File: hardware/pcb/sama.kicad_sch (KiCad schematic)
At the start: 19 parts, among them J4 Conn_ARM_JTAG_SWD_10, U1 SAMA7D65-4HB, Y1 32kHz768, Y2 24MHz

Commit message: bunch of small changes
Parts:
- added JP3: JTAGSEL, symbol Jumper:SolderJumper_3_Bridged12
- R10: value 4k02 ± 1% -> 4k02
- R2: value 240R 1% -> 240R
- R9: value 5k62 ± 1% -> 5k62
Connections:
- net +1V8_BATT_CPU: now also JP3.1 (A); no longer U1.E8 (VBAT)
- net +3V3: now also JP3.3 (B)
- net BOOT.DAT1: now reaches U1.A13 (PB25)
- net BOOT.DAT2: now reaches U1.A15 (PB26)
- net BOOT.DAT0: now reaches U1.B15 (PB24)
- net BOOT.DAT3: now reaches U1.C11 (PB27)
- net BOOT.CMD: now reaches U1.C14 (PB22)
- net BOOT.CK: now reaches U1.D14 (PB23)
- net BOOT.CD: now reaches U1.G4 (PB29)
- net EXT.DAT1: now reaches U1.P16 (PA4)
- net EXT.DAT3: now reaches U1.R12 (PA10)
- net EXT.DAT0: now reaches U1.T18 (PA3)
- net EXT.DAT2: now reaches U1.U14 (PA9)
- net EXT.CK: now reaches U1.U18 (PA0)
- net EXT.CD: now reaches U1.V15 (PA16)
- net EXT.CMD: now reaches U1.V17 (PA1)
- net UART_SAMBA_RX: now reaches U1.F18 (PD19)
- net UART_SAMBA_TX: now reaches U1.H16 (PD18)
- new net: JP3.2 (C), U1.E8 (VBAT)
- no-connect marks 27 -> 38
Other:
- moved on the sheet: U1D

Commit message: bunch of small audio and rf changes
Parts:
- added J8: Conn_01x02_Pin, symbol Connector:Conn_01x02_Pin
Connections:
- net UART_SAMBA_RX: now also J8.2 (Pin_2)
- net UART_SAMBA_TX: now also J8.1 (Pin_1)
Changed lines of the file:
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@@
+	)
+	(symbol
+		(lib_id "Connector:Conn_01x02_Pin")
+		(at 99.06 139.7 0)
+		(mirror y)
+		(unit 1)
+		(body_style 1)
+		(exclude_from_sim no)
+		(in_bom yes)
+		(on_board yes)
+		(in_pos_files yes)
+		(dnp no)
+		(property "Reference" "J8"
+			(at 96.266 136.398 0)
+			(show_name no)
+			(do_not_autoplace no)
+			(effects
+				(font
+					(size 1.27 1.27)
+				)
+			)
+		)
+		(property "Value" "Conn_01x02_Pin"
+			(at 100.33 142.2399 0)
+			(hide yes)
+			(show_name no)
+			(do_not_autoplace no)
+			(effects
+				(font
+					(size 1.27 1.27)
+				)
+				(justify right)
+			)
+		)
+		(property "Footprint" ""
+			(at 99.06 139.7 0)
+			(hide yes)
+			(show_name no)
+			(do_not_autoplace no)
+			(effects
+				(font
+					(size 1.27 1.27)
+				)
+			)
+		)
+		(property "Datasheet" ""
+			(at 99.06 139.7 0)
+			(hide yes)
+			(show_name no)
+			(do_not_autoplace no)
+			(effects
+				(font
+					(size 1.27 1.27)
+				)
+			)
+		)
+		(property "Description" "Generic connector, single row, 01x02, script generated"
+			(at 99.06 139.7 0)
+			(hide yes)
+			(show_name no)
+			(do_not_autoplace no)
+			(effects
+				(font
+					(size 1.27 1.27)
+				)
+			)
+		)
+		(pin "1"
+		)
+		(pin "2"
+		)
+		(instances
+			(project "meko"
+				(path "/da54f10a-146b-4941-a9c7-55c7173bb101/11193406-550a-48b1-a654-5418a2035a4e"
+					(reference "J8")
+					(unit 1)
+				)
+			)
+		)
 	)
 	(symbol

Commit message: replaced lpddr3 with ddr3l
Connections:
- net DDR_A14: now reaches U1.L9 (DDR_A14)
- net DDR_A11: now reaches U1.M9 (DDR_A11)
- net ~{WE}: now reaches U1.N10 (DDR_WEN)
- net BA1: now reaches U1.P4 (DDR_BA1)
- net DDR_A12: now reaches U1.P5 (DDR_A12)
- net BA2: now reaches U1.R8 (DDR_BA2)
- net DDR_A10: now reaches U1.T3 (DDR_A10)
- net ~{CAS}: now reaches U1.T8 (DDR_CASN)
- net ~{RAS}: now reaches U1.U8 (DDR_RASN)
- net ~{RESET}: now reaches U1.V1 (DDR_RESETN)
- net DDR_A13: now reaches U1.V2 (DDR_A13)
- net BA0: now reaches U1.V8 (DDR_BA0)
- net +1V2_DDR renamed +1V35_DDR
- no-connect marks 38 -> 26

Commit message: assigning pins
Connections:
- net +1V8: now also U1.F13 (VDDSDMMC2), U1.P19 (VDDQSPI0)
- net +3V3: now also U1.F9 (VDDSDMMC1), U1.W17 (VDDSDMMC0)
- net BT.HOST_WAKE: now reaches U1.L14 (PB19)
- net BT.DEV_WAKE: now reaches U1.M12 (PB20)
- net BT.DIN: now reaches U1.M14 (PB17)
- net BT.FSYNC: now reaches U1.M15 (PB15)
- net WL.EN: now reaches U1.N14 (PB13)
- net BT.BCLK: now reaches U1.N15 (PB14)
- net BT.DOUT: now reaches U1.N20 (PB16)
- net BT.MCLK: now reaches U1.N21 (PB18)
- net BT.CTSN: now reaches U1.P17 (PB10)
- net BT.RTSN: now reaches U1.P18 (PB12)
- net BT.RX: now reaches U1.R18 (PB9)
- net BT.EN: now reaches U1.R19 (PB11)
- net BT.TX: now reaches U1.T19 (PB8)
- net WIFI.DAT2: now reaches U1.A16 (PC31)
- net WIFI.DAT0: now reaches U1.B16 (PC29)
- net WIFI.CMD: now reaches U1.C15 (PC27)
- net WIFI.DAT3: now reaches U1.C16 (PD0)
- net WIFI.CK: now reaches U1.D16 (PC28)
- net WIFI.DAT1: now reaches U1.D17 (PC30)
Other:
- note added: "CTS"
- note added: "RTS"
- note added: "RX"
- note added: "TX"
- moved on the sheet: C27, J8, R10, R9, TP2, TP3, TP4, TP5, TP6, U1E, U1F

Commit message: connect everything up (Almost)
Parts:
- added R25, R36, R37, R40: 10k, symbol Device:R_Small
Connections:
- net +1V8: now also U1.C17 (VDDIOP1)
- net +3V3: now also U1.H19 (VDDGMAC1), U1.L19 (VDDGMAC0), U1.T13 (VDDIOP0), U1.W11 (VDDLVDS), R25.2, R36.2, R37.2, R40.2
- net CHG_~{INT}: now also U1.B19 (PD30)
- net CODEC.BCLK: now also U1.H4 (PC16)
- net CODEC.DIN: now also U1.D4 (PC17)
- net CODEC.DOUT: now also U1.J7 (PC14)
- net CODEC.FSYNC: now also U1.F3 (PC15)
- net DISP: now also U1.B21 (PA25)
- net FUEL_~{INT}: now also U1.F20 (PD31)
- net GPI1: now also U1.K9 (PD25)
- net GPIO1: now also U1.F19 (PD22)
- net GPIO2: now also U1.G18 (PD23)
- net GPO1: now also U1.G19 (PD24)
- net HAPT_EN: now also U1.Y19 (PE11)
- net HAPT_~{INT}: now also U1.AA19 (PE10)
- net HPM: now also U1.C1 (PC11)
- net SCL: now also U1.H6 (PC6), R37.1
- net SCLK: now also U1.P10 (PA22)
- net SCS: now also U1.AA20 (PA23)
- net SDA: now also U1.B1 (PC7), R40.1
- net SI: now also U1.P9 (PA24)
- net TOUCH.SCL: now also U1.K12 (PE2), R36.1
- net TOUCH.SDA: now also U1.D20 (PE3), R25.1
- net TOUCH_~{INT}: now also U1.Y15 (PE7)
- net TOUCH_~{RST}: now also U1.AA16 (PE8)
- net UART_SAMBA_RX: now also J8.1 (Pin_1), U1.H16 (PD18); no longer J8.2 (Pin_2), U1.F18 (PD19)
- net UART_SAMBA_TX: now also J8.2 (Pin_2), U1.F18 (PD19); no longer J8.1 (Pin_1), U1.H16 (PD18)
- net WL.DEV_WAKE: now also U1.G13 (PD2)
- net WL.HOST_WAKE: now also U1.A18 (PD1)
- net ~{DET}_2.5mm: now also U1.C2 (PC4)
- net ~{DET}_3.5mm: now also U1.G8 (PC3)
- net ~{INT}: now also U1.H5 (PC12)
- no-connect marks 26 -> 19
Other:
- note added: "DDR"
- note added: "GPIO"
- note added: "PERIs"
- note added: "PWR"
- note added: "SYS"
- moved on the sheet: C22, C23, C24, C25, C27, J4, J8, JP2, JP3, R10, R2, R9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

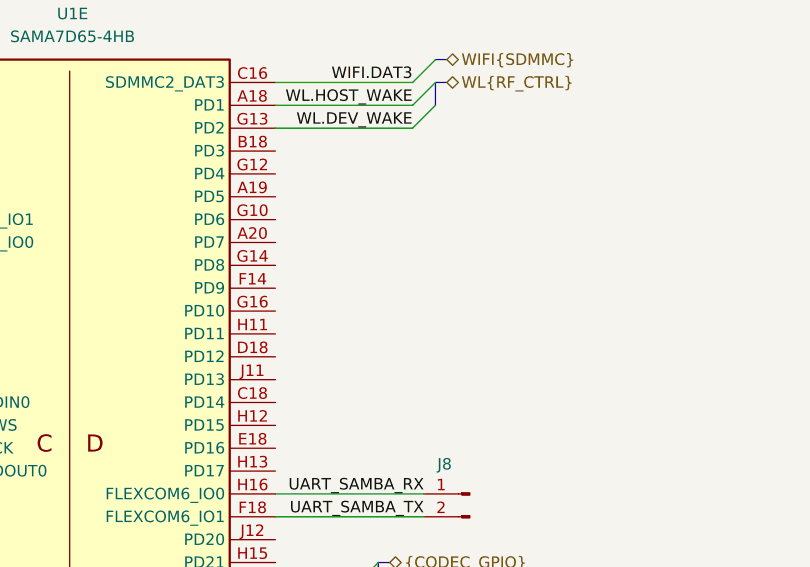
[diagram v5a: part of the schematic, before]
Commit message: added buttons
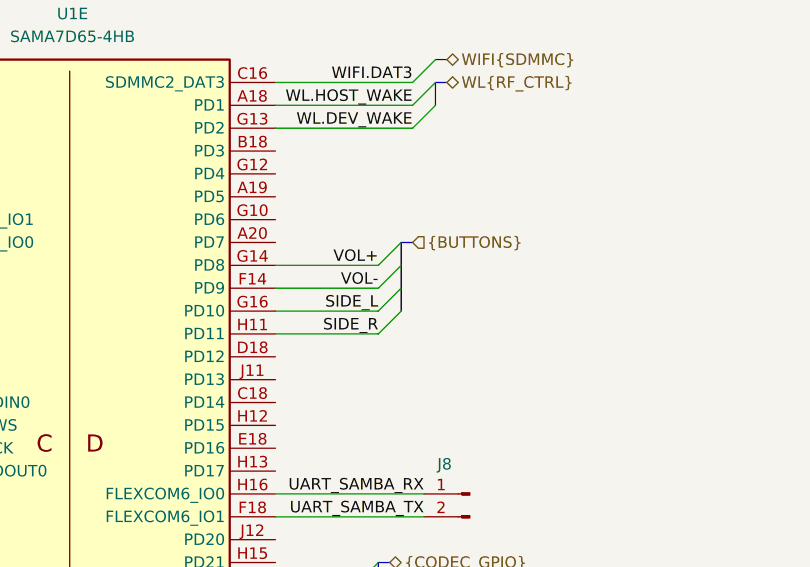
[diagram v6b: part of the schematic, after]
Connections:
- net VOL-: now reaches U1.F14 (PD9)
- net VOL+: now reaches U1.G14 (PD8)
- net SIDE_L: now reaches U1.G16 (PD10)
- net SIDE_R: now reaches U1.H11 (PD11)
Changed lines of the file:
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@@
 	)
 	(bus_entry
+		(at 130.81 73.66)
+		(size -2.54 2.54)
+		(stroke
+			(width 0)
+			(type default)
+		)
+	)
+	(bus_entry
 		(at 281.94 102.87)
 		(size -2.54 2.54)
@@
 	)
 	(bus_entry
+		(at 130.81 71.12)
+		(size -2.54 2.54)
+		(stroke
+			(width 0)
+			(type default)
+		)
+	)
+	(bus_entry
 		(at 463.55 107.95)
 		(size -2.54 2.54)
@@
 	)
 	(bus_entry
+		(at 130.81 68.58)
+		(size -2.54 2.54)
+		(stroke
+			(width 0)
+			(type default)
+		)
+	)
+	(bus_entry
 		(at 463.55 81.28)
 		(size -2.54 2.54)
@@
 	)
 	(bus_entry
+		(at 130.81 66.04)
+		(size -2.54 2.54)
+		(stroke
+			(width 0)
+			(type default)
+		)
+	)
+	(bus_entry
 		(at 463.55 68.58)
 		(size -2.54 2.54)
@@
 		)
 	)
+	(bus
+		(pts
+			(xy 130.81 66.04) (xy 130.81 73.66)
+		)
+		(stroke
+			(width 0)
+			(type default)
+		)
+	)
 	(wire
 		(pts
@@
 	(wire
 		(pts
+			(xy 116.84 73.66) (xy 128.27 73.66)
+		)
+		(stroke
+			(width 0)
+			(type default)
+		)
+	)
+	(wire
+		(pts
 			(xy 199.39 82.55) (xy 209.55 82.55)
 		)
@@
 	(bus
 		(pts
+			(xy 132.08 66.04) (xy 130.81 66.04)
+		)
+		(stroke
+			(width 0)
+			(type default)
+		)
+	)
+	(bus
+		(pts
 			(xy 283.21 74.93) (xy 281.94 74.93)
 		)
@@
 	(wire
 		(pts
+			(xy 116.84 71.12) (xy 128.27 71.12)
+		)
+		(stroke
+			(width 0)
+			(type default)
+		)
+	)
+	(wire
+		(pts
 			(xy 331.47 226.06) (xy 334.01 226.06)
 		)
@@
 	(wire
 		(pts
+			(xy 116.84 68.58) (xy 128.27 68.58)
+		)
+		(stroke
+			(width 0)
+			(type default)
+		)
+	)
+	(wire
+		(pts
 			(xy 151.13 227.33) (xy 165.1 227.33)
 		)
@@
 	(wire
 		(pts
+			(xy 116.84 76.2) (xy 128.27 76.2)
+		)
+		(stroke
+			(width 0)
+			(type default)
+		)
+	)
+	(wire
+		(pts
 			(xy 450.85 290.83) (xy 450.85 293.37)
 		)
@@
 		)
 	)
+	(label "SIDE_L"
+		(at 128.27 73.66 180)
+		(effects
+			(font
+				(size 1.27 1.27)
+			)
+			(justify right bottom)
+		)
+	)
 	(label "DQ5"
 		(at 461.01 68.58 180)
@@
 		)
 	)
+	(label "VOL-"
+		(at 128.27 71.12 180)
+		(effects
+			(font
+				(size 1.27 1.27)
+			)
+			(justify right bottom)
+		)
+	)
 	(label "DDR_A9"
 		(at 393.7 78.74 0)
@@
 		)
 	)
+	(label "VOL+"
+		(at 128.27 68.58 180)
+		(effects
+			(font
+				(size 1.27 1.27)
+			)
+			(justify right bottom)
+		)
+	)
 	(label "TDI"
 		(at 66.04 111.76 0)
@@
 		)
 	)
+	(label "SIDE_R"
+		(at 128.27 76.2 180)
+		(effects
+			(font
+				(size 1.27 1.27)
+			)
+			(justify right bottom)
+		)
+	)
 	(label "TDO"
 		(at 167.64 275.59 0)
@@
 		(effects
 			(font
+				(size 1.27 1.27)
+			)
+			(justify left)
+		)
+	)
+	(hierarchical_label "{BUTTONS}"
+		(shape input)
+		(at 132.08 66.04 0)
+		(effects
+			(font

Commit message: looking over stuff, added caps
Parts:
- added C100, C115, C119, C68, C83, C89, C90: 4u7, Capacitor_SMD:C_0402_1005Metric, symbol Device:C_Small
- added C101, C102, C103, C104, C105, C106, C107, C108, C109, C110, C111, C112, C113, C114, C116, C117, C118, C120, C121, C122, C123, C124, C125, C69, C70, C71, C72, C73, C74, C75, C76, C77, C78, C79, C80, C81, C82, C84, C85, C86, C87, C88, C91, C92, C93, C94, C95, C96, C97, C98, C99: 100n, Capacitor_SMD:C_0402_1005Metric, symbol Device:C_Small
- added R45, R46, R47, R48: 16k9, Resistor_SMD:R_0402_1005Metric, symbol Device:R_Small
- added TP7: ~{TRST}, symbol Connector:TestPoint
- C22, C23, C24, C25, C27: footprint (none) -> Capacitor_SMD:C_0402_1005Metric
- R10, R2, R25, R36, R37, R40, R9: footprint (none) -> Resistor_SMD:R_0402_1005Metric
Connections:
- net +1V15_CORE: now also C68.1, C69.1, C70.1, C71.1, C72.1, C73.1, C74.1, C75.1, C76.1, C77.1, C78.1, C79.1, C80.1, C81.1, C82.1
- net +1V15_CPU: now also C83.1, C84.1, C85.1, C86.1, C87.1, C88.1
- net +1V35_DDR: now also C100.1, C101.1, C102.1, C103.1, C104.1, C105.1, C106.1, C107.1, C108.1, C109.1, C110.1, C111.1, C112.1, C113.1, C114.1
- net +1V8: now also C115.1, C116.1, C117.1, C118.1
- net +3V3: now also C90.1, C91.1, C92.1, C93.1, C94.1, C95.1, C96.1, C97.1, C98.1
- net GND: now also C100.2, C101.2, C102.2, C103.2, C104.2, C105.2, C106.2, C107.2, C108.2, C109.2, C110.2, C111.2, C112.2, C113.2, C114.2, C115.2, C116.2, C117.2, C118.2, C119.2, C120.2, C121.2, C122.2, C123.2, C124.2, C125.2, C68.2, C69.2, C70.2, C71.2, C72.2, C73.2, C74.2, C75.2, C76.2, C77.2, C78.2, C79.2, C80.2, C81.2, C82.2, C83.2, C84.2, C85.2, C86.2, C87.2, C88.2, C90.2, C91.2, C92.2, C93.2, C94.2, C95.2, C96.2, C97.2, C98.2, C99.2, R45.1, R46.1, R47.1, R48.1
- net +2V5: now reaches U1.D2 (ADVREFP)
- net +2V5: now also U1.E3 (VDDOUT25), U1.E5 (VDDANA), U1.J6 (VDDANA), U1.T16 (VDDDPHY), U1.W14 (VDDIN25), C119.1, C120.1, C121.1, C122.1, C123.1, C124.1, C125.1
- net VBAT: now reaches JP3.2 (C), U1.E8 (VBAT)
- net VBAT: now also C99.1
- net at U1.B13 (SDMMC1_CAL): now also R46.2
- net at U1.E14 (SDMMC2_CAL): now also R47.2
- net at U1.K8 (AUDIOCLK): now also TP7.1
- net at U1.M13 (QSPI0_CAL): now also R48.2
- net at U1.R16 (SDMMC0_CAL): now also R45.2

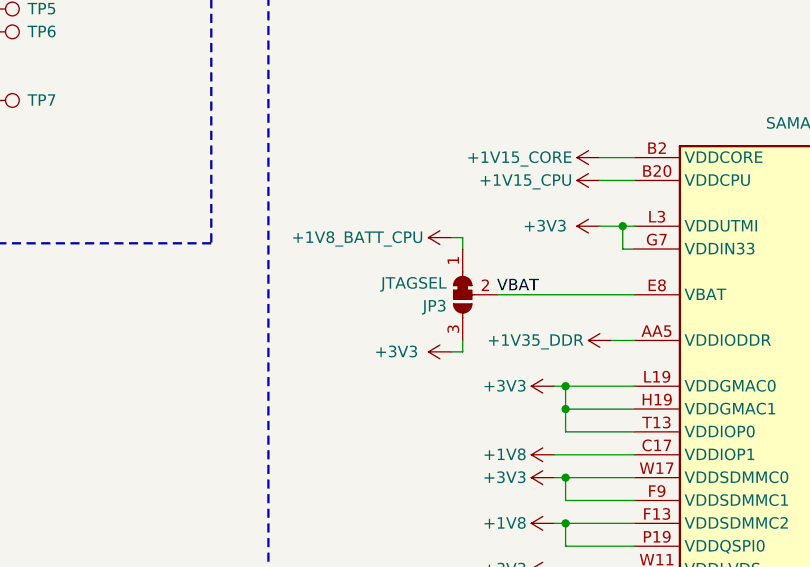
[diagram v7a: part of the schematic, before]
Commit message: added bq25640 footprint
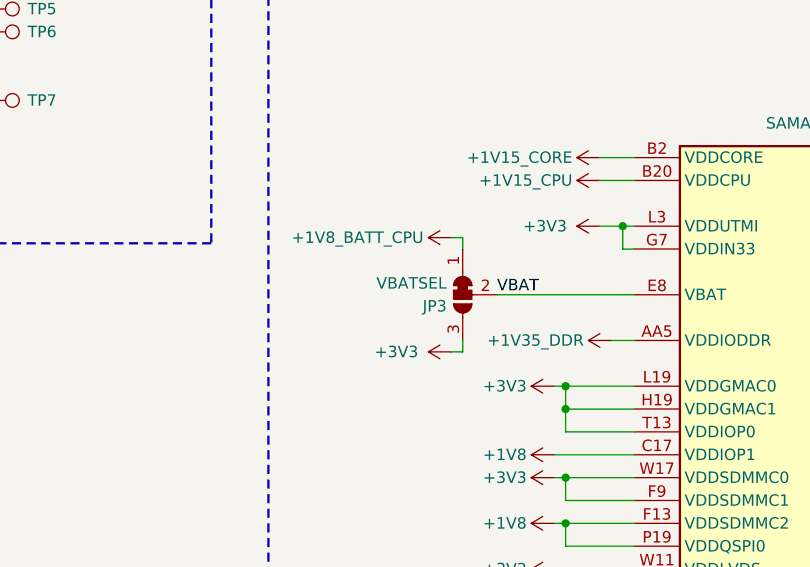
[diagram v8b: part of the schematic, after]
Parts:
- JP3: value JTAGSEL -> VBATSEL
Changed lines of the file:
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@@
 			)
 		)
-		(property "Value" "JTAGSEL"
+		(property "Value" "VBATSEL"
 			(at 385.572 256.54 90)
 			(show_name no)
